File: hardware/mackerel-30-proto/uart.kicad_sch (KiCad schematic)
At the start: 9 parts, among them J4 Conn_01x06, J5 Conn_01x06, J6 Conn_02x10_Odd_Even, U5 XR68C681, X2 3.6864MHz

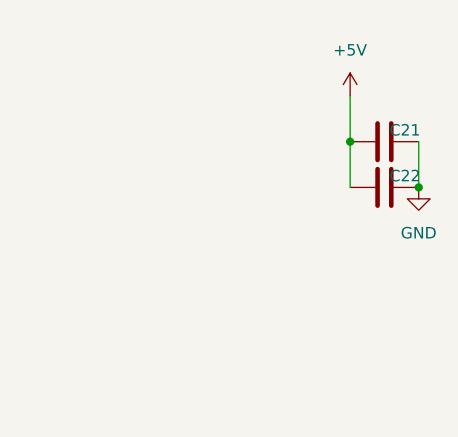
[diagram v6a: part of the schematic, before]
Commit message: Mack-30 routed except for expansion header
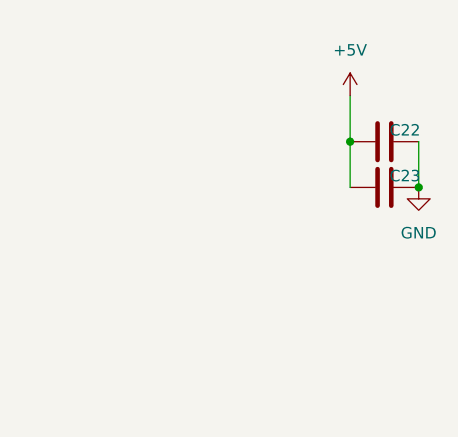
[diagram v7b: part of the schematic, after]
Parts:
- renumbered C21 to C22, C22 to C23
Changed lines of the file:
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@@
 		(dnp no)
 		(fields_autoplaced yes)
-		(property "Reference" "#PWR038"
+		(property "Reference" "#PWR040"
 			(at 232.41 39.37 0)
 			(effects
@@
 			(project "mackerel-30-proto"
 				(path "/9307474f-ec99-494d-b4c9-fbd0b10ce86a/d143ddc0-b4a1-490e-ae52-7a0ad9150902"
-					(reference "#PWR038")
+					(reference "#PWR040")
 					(unit 1)
 				)
@@
 		(on_board yes)
 		(dnp no)
-		(property "Reference" "#PWR026"
+		(property "Reference" "#PWR028"
 			(at 73.66 114.3 0)
 			(effects
@@
 			(project "mackerel-30-proto"
 				(path "/9307474f-ec99-494d-b4c9-fbd0b10ce86a/d143ddc0-b4a1-490e-ae52-7a0ad9150902"
-					(reference "#PWR026")
+					(reference "#PWR028")
 					(unit 1)
 				)
@@
 		(dnp no)
 		(fields_autoplaced yes)
-		(property "Reference" "#PWR025"
+		(property "Reference" "#PWR027"
 			(at 31.75 62.23 0)
 			(effects
@@
 			(project "mackerel-30-proto"
 				(path "/9307474f-ec99-494d-b4c9-fbd0b10ce86a/d143ddc0-b4a1-490e-ae52-7a0ad9150902"
-					(reference "#PWR025")
+					(reference "#PWR027")
 					(unit 1)
 				)
@@
 		(on_board yes)
 		(dnp no)
-		(property "Reference" "#PWR027"
+		(property "Reference" "#PWR029"
 			(at 73.66 132.08 0)
 			(effects
@@
 			(project "mackerel-30-proto"
 				(path "/9307474f-ec99-494d-b4c9-fbd0b10ce86a/d143ddc0-b4a1-490e-ae52-7a0ad9150902"
-					(reference "#PWR027")
+					(reference "#PWR029")
 					(unit 1)
 				)
@@
 		(dnp no)
 		(fields_autoplaced yes)
-		(property "Reference" "#PWR030"
+		(property "Reference" "#PWR032"
 			(at 139.7 144.78 0)
 			(effects
@@
 			(project "mackerel-30-proto"
 				(path "/9307474f-ec99-494d-b4c9-fbd0b10ce86a/d143ddc0-b4a1-490e-ae52-7a0ad9150902"
-					(reference "#PWR030")
+					(reference "#PWR032")
 					(unit 1)
 				)
@@
 		(dnp no)
 		(fields_autoplaced yes)
-		(property "Reference" "#PWR036"
+		(property "Reference" "#PWR038"
 			(at 228.6 83.82 0)
 			(effects
@@
 			(project "mackerel-30-proto"
 				(path "/9307474f-ec99-494d-b4c9-fbd0b10ce86a/d143ddc0-b4a1-490e-ae52-7a0ad9150902"
-					(reference "#PWR036")
+					(reference "#PWR038")
 					(unit 1)
 				)
@@
 		(dnp no)
 		(fields_autoplaced yes)
-		(property "Reference" "#PWR040"
+		(property "Reference" "#PWR042"
 			(at 240.03 86.36 0)
 			(effects
@@
 			(project "mackerel-30-proto"
 				(path "/9307474f-ec99-494d-b4c9-fbd0b10ce86a/d143ddc0-b4a1-490e-ae52-7a0ad9150902"
-					(reference "#PWR040")
+					(reference "#PWR042")
 					(unit 1)
 				)
@@
 		(dnp no)
 		(fields_autoplaced yes)
-		(property "Reference" "#PWR028"
+		(property "Reference" "#PWR030"
 			(at 106.68 106.68 0)
 			(effects
@@
 			(project "mackerel-30-proto"
 				(path "/9307474f-ec99-494d-b4c9-fbd0b10ce86a/d143ddc0-b4a1-490e-ae52-7a0ad9150902"
-					(reference "#PWR028")
+					(reference "#PWR030")
 					(unit 1)
 				)
@@
 		(dnp no)
 		(fields_autoplaced yes)
-		(property "Reference" "#PWR041"
+		(property "Reference" "#PWR043"
 			(at 240.03 91.44 0)
 			(effects
@@
 			(project "mackerel-30-proto"
 				(path "/9307474f-ec99-494d-b4c9-fbd0b10ce86a/d143ddc0-b4a1-490e-ae52-7a0ad9150902"
-					(reference "#PWR041")
+					(reference "#PWR043")
 					(unit 1)
 				)
@@
 		(dnp no)
 		(fields_autoplaced yes)
-		(property "Reference" "#PWR024"
+		(property "Reference" "#PWR026"
 			(at 31.75 35.56 0)
 			(effects
@@
 			(project "mackerel-30-proto"
 				(path "/9307474f-ec99-494d-b4c9-fbd0b10ce86a/d143ddc0-b4a1-490e-ae52-7a0ad9150902"
-					(reference "#PWR024")
+					(reference "#PWR026")
 					(unit 1)
 				)
@@
 		(dnp no)
 		(fields_autoplaced yes)
-		(property "Reference" "#PWR033"
+		(property "Reference" "#PWR035"
 			(at 204.47 91.44 0)
 			(effects
@@
 			(project "mackerel-30-proto"
 				(path "/9307474f-ec99-494d-b4c9-fbd0b10ce86a/d143ddc0-b4a1-490e-ae52-7a0ad9150902"
-					(reference "#PWR033")
+					(reference "#PWR035")
 					(unit 1)
 				)
@@
 		(on_board yes)
 		(dnp no)
-		(property "Reference" "C21"
+		(property "Reference" "C22"
 			(at 238.506 39.37 90)
 			(effects
@@
 			(project "mackerel-30-proto"
 				(path "/9307474f-ec99-494d-b4c9-fbd0b10ce86a/d143ddc0-b4a1-490e-ae52-7a0ad9150902"
-					(reference "C21")
+					(reference "C22")
 					(unit 1)
 				)
@@
 		(dnp no)
 		(fields_autoplaced yes)
-		(property "Reference" "#PWR037"
+		(property "Reference" "#PWR039"
 			(at 228.6 109.22 0)
 			(effects
@@
 			(project "mackerel-30-proto"
 				(path "/9307474f-ec99-494d-b4c9-fbd0b10ce86a/d143ddc0-b4a1-490e-ae52-7a0ad9150902"
-					(reference "#PWR037")
+					(reference "#PWR039")
 					(unit 1)
 				)
@@
 		(dnp no)
 		(fields_autoplaced yes)
-		(property "Reference" "#PWR039"
+		(property "Reference" "#PWR041"
 			(at 240.03 52.07 0)
 			(effects
@@
 			(project "mackerel-30-proto"
 				(path "/9307474f-ec99-494d-b4c9-fbd0b10ce86a/d143ddc0-b4a1-490e-ae52-7a0ad9150902"
-					(reference "#PWR039")
+					(reference "#PWR041")
 					(unit 1)
 				)
@@
 		(dnp no)
 		(fields_autoplaced yes)
-		(property "Reference" "#PWR031"
+		(property "Reference" "#PWR033"
 			(at 167.64 116.84 0)
 			(effects
@@
 			(project "mackerel-30-proto"
 				(path "/9307474f-ec99-494d-b4c9-fbd0b10ce86a/d143ddc0-b4a1-490e-ae52-7a0ad9150902"
-					(reference "#PWR031")
+					(reference "#PWR033")
 					(unit 1)
 				)
@@
 		(on_board yes)
 		(dnp no)
-		(property "Reference" "#PWR029"
+		(property "Reference" "#PWR031"
 			(at 139.7 63.5 0)
 			(effects
@@
 			(project "mackerel-30-proto"
 				(path "/9307474f-ec99-494d-b4c9-fbd0b10ce86a/d143ddc0-b4a1-490e-ae52-7a0ad9150902"
-					(reference "#PWR029")
+					(reference "#PWR031")
 					(unit 1)
 				)
@@
 		(on_board yes)
 		(dnp no)
-		(property "Reference" "C22"
+		(property "Reference" "C23"
 			(at 238.506 44.45 90)
 			(effects
@@
 			(project "mackerel-30-proto"
 				(path "/9307474f-ec99-494d-b4c9-fbd0b10ce86a/d143ddc0-b4a1-490e-ae52-7a0ad9150902"
-					(reference "C22")
+					(reference "C23")
 					(unit 1)
 				)
@@
 		(dnp no)
 		(fields_autoplaced yes)
-		(property "Reference" "#PWR035"
+		(property "Reference" "#PWR037"
 			(at 215.9 109.22 0)
 			(effects
@@
 			(project "mackerel-30-proto"
 				(path "/9307474f-ec99-494d-b4c9-fbd0b10ce86a/d143ddc0-b4a1-490e-ae52-7a0ad9150902"
-					(reference "#PWR035")
+					(reference "#PWR037")
 					(unit 1)
 				)
@@
 		(dnp no)
 		(fields_autoplaced yes)
-		(property "Reference" "#PWR034"
+		(property "Reference" "#PWR036"
 			(at 215.9 83.82 0)
 			(effects
@@
 			(project "mackerel-30-proto"
 				(path "/9307474f-ec99-494d-b4c9-fbd0b10ce86a/d143ddc0-b4a1-490e-ae52-7a0ad9150902"
-					(reference "#PWR034")
+					(reference "#PWR036")
 					(unit 1)
 				)
@@
 		(dnp no)
 		(fields_autoplaced yes)
-		(property "Reference" "#PWR032"
+		(property "Reference" "#PWR034"
 			(at 204.47 86.36 0)
 			(effects
@@
 			(project "mackerel-30-proto"
 				(path "/9307474f-ec99-494d-b4c9-fbd0b10ce86a/d143ddc0-b4a1-490e-ae52-7a0ad9150902"
-					(reference "#PWR032")
-					(unit 1)
-				)
+					(reference "#PWR034")
+					(unit 1)
+				)

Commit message: PCB cleanup
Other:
- company: (none) -> Colin Maykish
- title: (none) -> Mackerel-30
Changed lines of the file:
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@@
 	(generator_version "8.0")
 	(paper "A")
+	(title_block
+		(title "Mackerel-30")
+		(date "2024-11-09")
+		(rev "0.1")
+		(company "Colin Maykish")
+	)
 	(junction
 		(at 106.68 110.49)
